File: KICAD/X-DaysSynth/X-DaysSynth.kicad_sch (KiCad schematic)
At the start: 23 parts, among them J1 STYLUS, J2 Power Switch, J3 AudioJackX_Ground_Switch, J4 LED Ring, J5 PATCH SELECT, J6 WRITE PATCH, J7 PARAM SELECT, J8 MODE, J9 Power, U1 stm32f103c8t6-module-china

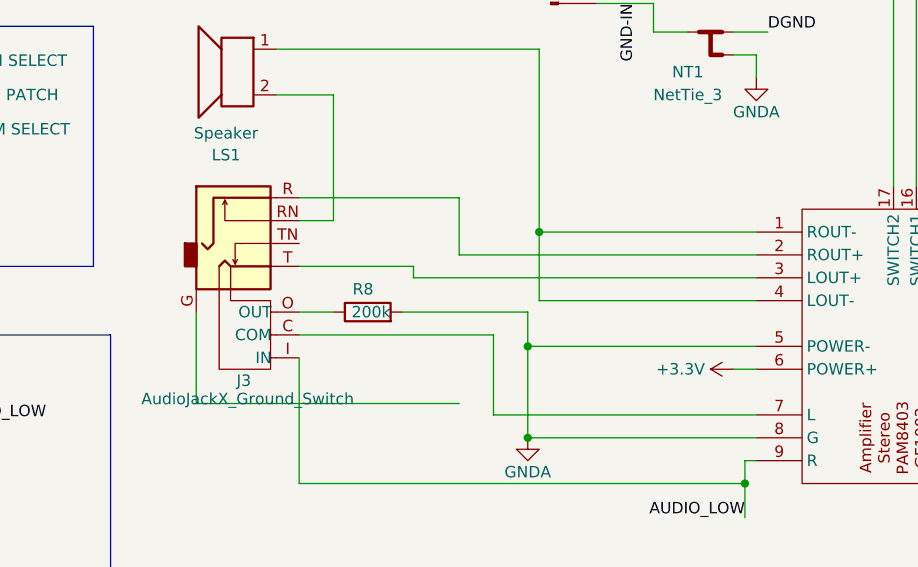
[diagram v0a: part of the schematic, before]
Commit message: LED ring 3d models updated PCB and schematic Logo Text first draft enclosures 3d models
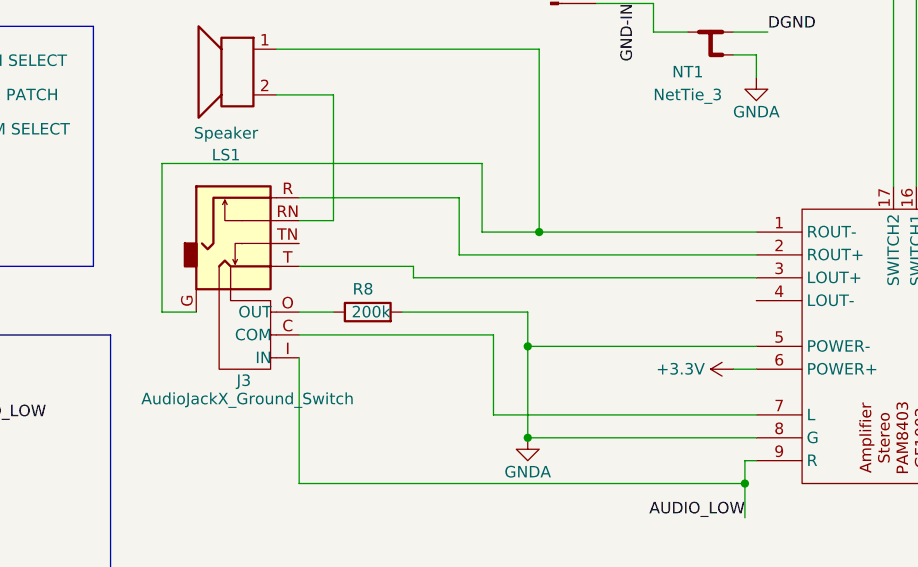
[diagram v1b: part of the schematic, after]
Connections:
- net at AMP1.1 (ROUT-), LS1.1: now also J3.G; no longer AMP1.4 (LOUT-)
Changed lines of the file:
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@@
-	(wire
-		(pts
-			(xy 101.6 152.4) (xy 101.6 162.56)
-		)
-		(stroke
-			(width 0)
-			(type default)
-		)
-	)
 	(wire
 		(pts
@@
 	(wire
 		(pts
+			(xy 133.35 143.51) (xy 139.7 143.51)
+		)
+		(stroke
+			(width 0)
+			(type default)
+		)
+	)
+	(wire
+		(pts
 			(xy 171.45 36.83) (xy 171.45 50.8)
 		)
@@
 	(wire
 		(pts
+			(xy 133.35 135.89) (xy 133.35 143.51)
+		)
+		(stroke
+			(width 0)
+			(type default)
+		)
+	)
+	(wire
+		(pts
 			(xy 72.39 63.5) (xy 78.74 63.5)
 		)
@@
 	(wire
 		(pts
-			(xy 101.6 162.56) (xy 130.81 162.56)
+			(xy 97.79 135.89) (xy 133.35 135.89)
 		)
 		(stroke
@@
 	(wire
 		(pts
+			(xy 97.79 152.4) (xy 101.6 152.4)
+		)
+		(stroke
+			(width 0)
+			(type default)
+		)
+	)
+	(wire
+		(pts
 			(xy 135.89 33.02) (xy 135.89 31.75)
 		)
@@
 	(wire
 		(pts
-			(xy 139.7 143.51) (xy 139.7 151.13)
-		)
-		(stroke
-			(width 0)
-			(type default)
-		)
-	)
-	(wire
-		(pts
 			(xy 138.43 156.21) (xy 163.83 156.21)
 		)
@@
 	(wire
 		(pts
+			(xy 97.79 135.89) (xy 97.79 152.4)
+		)
+		(stroke
+			(width 0)
+			(type default)
+		)
+	)
+	(wire
+		(pts
 			(xy 130.81 146.05) (xy 163.83 146.05)
 		)
@@
 		)
 		(stroke
-			(width 0)
-			(type default)
-		)
-	)
-	(wire
-		(pts
-			(xy 163.83 151.13) (xy 139.7 151.13)
-		)
-		(stroke
